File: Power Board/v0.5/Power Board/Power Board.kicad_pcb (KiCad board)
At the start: 4 copper layers, 70 x 80 mm, 91 parts, among them J1 Battery In, J2 JST B2PS-VH, J3 JST B2PS-VH, J4 JST B2PS-VH, J5 JST B2PS-VH, J6 JST B2PS-VH, J7 JST B2PS-VH, J9 Raspberry Pi, Q1 SI5504BDC, SW1 SW_Push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

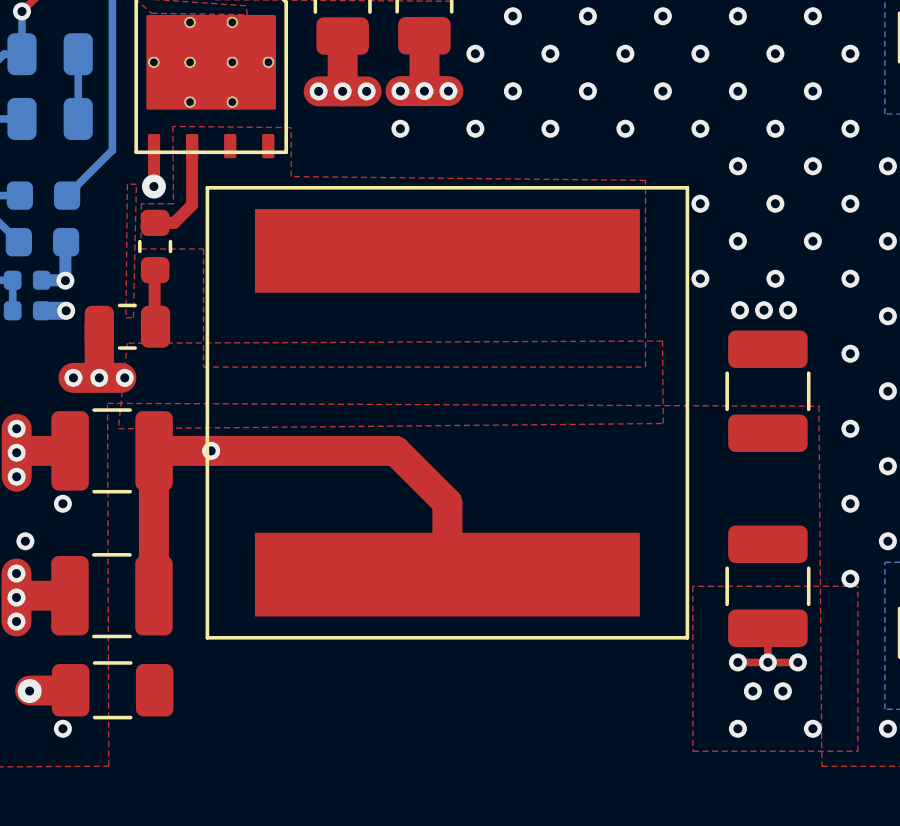
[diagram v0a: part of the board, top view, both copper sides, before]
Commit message: Correct Coilcraft XAL1580 footprint: enlarge pads, break up paste areas.
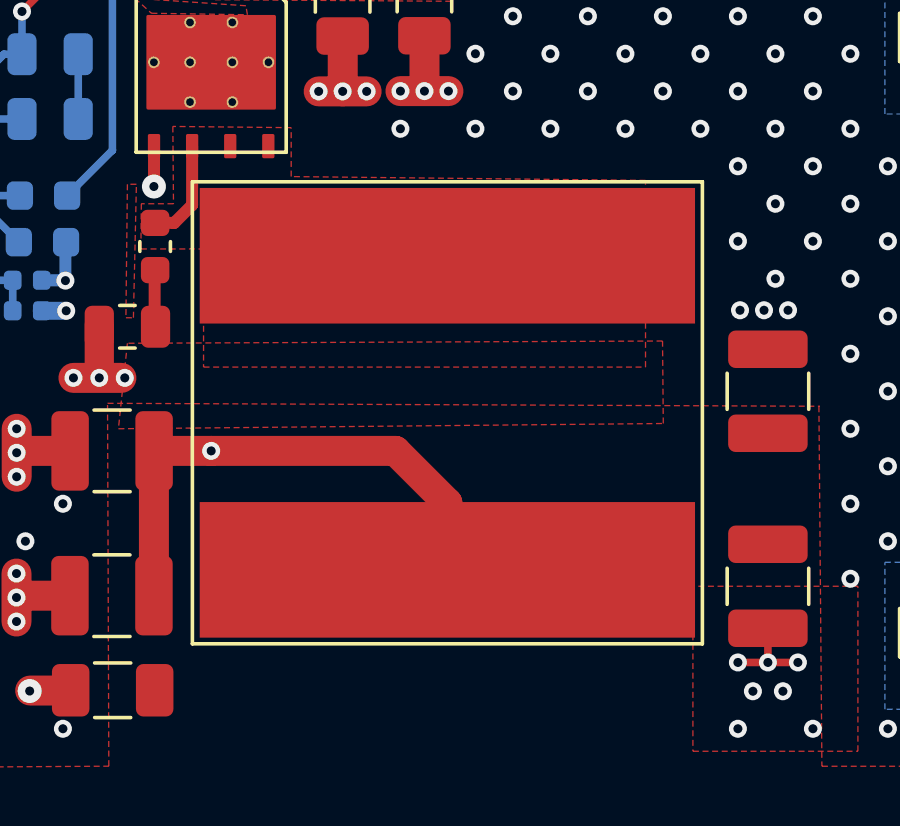
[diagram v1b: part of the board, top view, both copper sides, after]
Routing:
- net GND: vias 272 -> 270
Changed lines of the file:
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@@
     (thickness 1.6)
     (drawings 25)
-    (tracks 900)
+    (tracks 898)
     (zones 0)
     (modules 91)
@@
     (1 In1.Cu signal)
     (2 In2.Cu signal)
-    (31 B.Cu signal)
+    (31 B.Cu signal hide)
     (32 B.Adhes user hide)
     (33 F.Adhes user hide)
@@
     (35 F.Paste user hide)
     (36 B.SilkS user)
-    (37 F.SilkS user hide)
+    (37 F.SilkS user)
     (38 B.Mask user)
     (39 F.Mask user hide)
@@
     (45 Margin user hide)
     (46 B.CrtYd user)
-    (47 F.CrtYd user hide)
+    (47 F.CrtYd user)
     (48 B.Fab user hide)
     (49 F.Fab user hide)
@@
     (pad_to_mask_clearance 0.0508)
     (aux_axis_origin 0 0)
-    (visible_elements FFFFEFFF)
+    (visible_elements FFFEEFFF)
     (pcbplotparams
       (layerselection 0x010f0_ffffffff)
@@
     (add_net /Panel_Power)
   )
+  (module Power_Board:Coilcraft_XAL1580 (layer F.Cu)
+    (at 115.316 93.218 90)
+    (fp_text reference L8 (at 0 5.08 90) (layer F.SilkS) hide
+      (effects (font (size 1 1) (thickness 0.15)))
+    )
+    (fp_text value 1.3µH (at 0 -5.08 90) (layer F.Fab)
+      (effects (font (size 1 1) (thickness 0.15)))
+    )
+    (fp_line (start 8 8.8) (end 8 -8.8) (layer F.CrtYd) (width 0.12))
+    (fp_line (start -8 8.8) (end 8 8.8) (layer F.CrtYd) (width 0.12))
+    (fp_line (start -8 -8.8) (end -8 8.8) (layer F.CrtYd) (width 0.12))
+    (fp_line (start 8 -8.8) (end -8 -8.8) (layer F.CrtYd) (width 0.12))
+    (fp_line (start 7.7 8.5) (end 7.7 -8.5) (layer F.SilkS) (width 0.12))
+    (fp_line (start -7.7 8.5) (end 7.7 8.5) (layer F.SilkS) (width 0.12))
+    (fp_line (start -7.7 -8.5) (end -7.7 8.5) (layer F.SilkS) (width 0.12))
+    (fp_line (start 7.7 -8.5) (end -7.7 -8.5) (layer F.SilkS) (width 0.12))
+    (pad 2 smd roundrect (at -5.235 6.19125 90) (size 3 3) (layers F.Cu F.Paste) (roundrect_rratio 0.25)
+      (net 13 /Panel_Power))
+    (pad 2 smd roundrect (at -5.235 2.05 90) (size 3 3) (layers F.Cu F.Paste) (roundrect_rratio 0.25)
+      (net 13 /Panel_Power))
+    (pad 2 smd roundrect (at -5.235 -2.0635 90) (size 3 3) (layers F.Cu F.Paste) (roundrect_rratio 0.25)
+      (net 13 /Panel_Power))
+    (pad 2 smd roundrect (at -5.235 -6.1915 90) (size 3 3) (layers F.Cu F.Paste) (roundrect_rratio 0.25)
+      (net 13 /Panel_Power))
+    (pad 1 smd roundrect (at 5.235 6.19135 90) (size 3 3) (layers F.Cu F.Paste) (roundrect_rratio 0.25)
+      (net 41 "/Panel Power/Switch_Node"))
+    (pad 1 smd roundrect (at 5.235 2.06375 90) (size 3 3) (layers F.Cu F.Paste) (roundrect_rratio 0.25)
+      (net 41 "/Panel Power/Switch_Node"))
+    (pad 1 smd roundrect (at 5.235 -2.0635 90) (size 3 3) (layers F.Cu F.Paste) (roundrect_rratio 0.25)
+      (net 41 "/Panel Power/Switch_Node"))
+    (pad 1 smd roundrect (at 5.235 -6.1915 90) (size 3 3) (layers F.Cu F.Paste) (roundrect_rratio 0.25)
+      (net 41 "/Panel Power/Switch_Node"))
+    (pad 2 smd rect (at -5.235 0 90) (size 4.52 16.51) (layers F.Cu F.Mask)
+      (net 13 /Panel_Power))
+    (pad 1 smd rect (at 5.235 0 90) (size 4.52 16.51) (layers F.Cu F.Mask)
+      (net 41 "/Panel Power/Switch_Node"))
+    (model "${KIPRJMOD}/../Power Board Models/Coilcraft-XAL1580-102.step"
+      (at (xyz 0 0 0))
+      (scale (xyz 1 1 1))
+      (rotate (xyz -90 0 180))
+    )
+  )
   (module Resistor_SMD:R_0603_1608Metric (layer B.Cu)
     (at 93.25 89 180)
@@
       (xy -10.406932 -8.555676)) (layer B.Mask) (width 0.01))
   )
-  (module Power_Board:Coilcraft_XAL1580 (layer F.Cu)
-    (at 115.316 93.218 90)
-    (fp_text reference L8 (at 0 5.08 90) (layer F.SilkS) hide
-      (effects (font (size 1 1) (thickness 0.15)))
-    )
-    (fp_text value 1.3µH (at 0 -5.08 90) (layer F.Fab)
-      (effects (font (size 1 1) (thickness 0.15)))
-    )
-    (fp_line (start 7.75 8.25) (end 7.75 -8.25) (layer F.CrtYd) (width 0.12))
-    (fp_line (start -7.75 8.25) (end 7.75 8.25) (layer F.CrtYd) (width 0.12))
-    (fp_line (start -7.75 -8.25) (end -7.75 8.25) (layer F.CrtYd) (width 0.12))
-    (fp_line (start 7.75 -8.25) (end -7.75 -8.25) (layer F.CrtYd) (width 0.12))
-    (fp_line (start 7.5 8) (end 7.5 -8) (layer F.SilkS) (width 0.12))
-    (fp_line (start -7.5 8) (end 7.5 8) (layer F.SilkS) (width 0.12))
-    (fp_line (start -7.5 -8) (end -7.5 8) (layer F.SilkS) (width 0.12))
-    (fp_line (start 7.5 -8) (end -7.5 -8) (layer F.SilkS) (width 0.12))
-    (pad 2 smd rect (at -5.395 0 90) (size 2.79 12.83) (layers F.Cu F.Paste F.Mask)
-      (net 13 /Panel_Power))
-    (pad 1 smd rect (at 5.395 0 90) (size 2.79 12.83) (layers F.Cu F.Paste F.Mask)
-      (net 41 "/Panel Power/Switch_Node"))
-    (model "${KIPRJMOD}/../Power Board Models/Coilcraft-XAL1580-102.step"
-      (at (xyz 0 0 0))
-      (scale (xyz 1 1 1))
-      (rotate (xyz -90 0 180))
-    )
-  )
   (module Power_Board:Fuse_1206_3216Metric (layer F.Cu)
     (at 138.2 91.3)
@@
   (via (at 133.75 88.75) (size 0.6) (drill 0.3) (layers F.Cu B.Cu) (net 4))
   (via (at 126.25 88.75) (size 0.6) (drill 0.3) (layers F.Cu B.Cu) (net 4))
-  (via (at 123.75 88.75) (size 0.6) (drill 0.3) (layers F.Cu B.Cu) (net 4))
   (via (at 125 87.5) (size 0.6) (drill 0.3) (layers F.Cu B.Cu) (net 4))
   (via (at 127.5 87.5) (size 0.6) (drill 0.3) (layers F.Cu B.Cu) (net 4))
@@
   (via (at 128.75 86.25) (size 0.6) (drill 0.3) (layers F.Cu B.Cu) (net 4))
   (via (at 126.25 86.25) (size 0.6) (drill 0.3) (layers F.Cu B.Cu) (net 4))
-  (via (at 123.75 86.25) (size 0.6) (drill 0.3) (layers F.Cu B.Cu) (net 4))
   (via (at 125 85) (size 0.6) (drill 0.3) (layers F.Cu B.Cu) (net 4))
   (via (at 127.5 85) (size 0.6) (drill 0.3) (layers F.Cu B.Cu) (net 4))

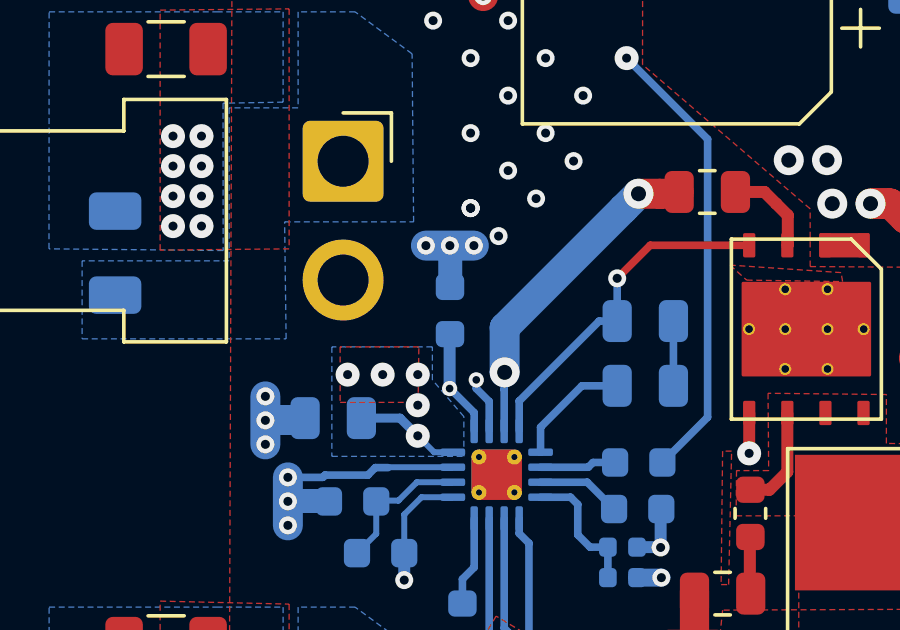
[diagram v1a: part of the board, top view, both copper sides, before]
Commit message: Correct C14 footprint, remove C6 and C9 incorrect package.
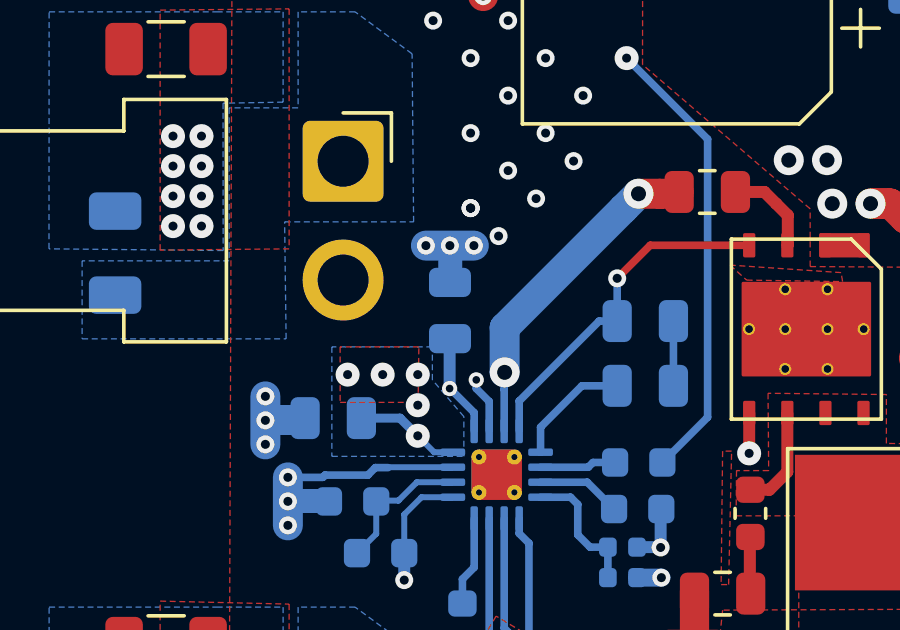
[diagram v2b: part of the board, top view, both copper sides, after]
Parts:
- C14: footprint Capacitor_SMD:C_0603_1608Metric -> Capacitor_SMD:C_0805_2012Metric
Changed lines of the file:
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@@
   (layers
     (0 F.Cu signal)
-    (1 In1.Cu signal)
-    (2 In2.Cu signal)
-    (31 B.Cu signal hide)
+    (1 In1.Cu signal hide)
+    (2 In2.Cu signal hide)
+    (31 B.Cu signal)
     (32 B.Adhes user hide)
     (33 F.Adhes user hide)
@@
     (pad_to_mask_clearance 0.0508)
     (aux_axis_origin 0 0)
-    (visible_elements FFFEEFFF)
+    (visible_elements FFFFEFFF)
     (pcbplotparams
       (layerselection 0x010f0_ffffffff)
@@
     (add_net /Panel_Power)
   )
+  (module Capacitor_SMD:C_0805_2012Metric (layer B.Cu)
+    (at 95.563 80.914 90)
+    (descr "Capacitor SMD 0805 (2012 Metric), square (rectangular) end terminal, IPC_7351 nominal, (Body size source: https://docs.google.com/spreadsheets/d/1BsfQQcO9C6DZCsRaXUlFlo91Tg2WpOkGARC1WS5S8t0/edit?usp=sharing), generated with kicad-footprint-generator")
+    (tags capacitor)
+    (attr smd)
+    (fp_text reference C14 (at 0 1.65 90) (layer B.SilkS)
+      (effects (font (size 1 1) (thickness 0.15)) (justify mirror))
+    )
+    (fp_text value 1µF (at 0 -1.65 90) (layer B.Fab)
+      (effects (font (size 1 1) (thickness 0.15)) (justify mirror))
+    )
+    (fp_text user %R (at 0 0 90) (layer B.Fab)
+      (effects (font (size 0.5 0.5) (thickness 0.08)) (justify mirror))
+    )
+    (fp_line (start 1.68 -0.95) (end -1.68 -0.95) (layer B.CrtYd) (width 0.05))
+    (fp_line (start 1.68 0.95) (end 1.68 -0.95) (layer B.CrtYd) (width 0.05))
+    (fp_line (start -1.68 0.95) (end 1.68 0.95) (layer B.CrtYd) (width 0.05))
+    (fp_line (start -1.68 -0.95) (end -1.68 0.95) (layer B.CrtYd) (width 0.05))
+    (fp_line (start -0.258578 -0.71) (end 0.258578 -0.71) (layer B.SilkS) (width 0.12))
+    (fp_line (start -0.258578 0.71) (end 0.258578 0.71) (layer B.SilkS) (width 0.12))
+    (fp_line (start 1 -0.6) (end -1 -0.6) (layer B.Fab) (width 0.1))
+    (fp_line (start 1 0.6) (end 1 -0.6) (layer B.Fab) (width 0.1))
+    (fp_line (start -1 0.6) (end 1 0.6) (layer B.Fab) (width 0.1))
+    (fp_line (start -1 -0.6) (end -1 0.6) (layer B.Fab) (width 0.1))
+    (pad 2 smd roundrect (at 0.9375 0 90) (size 0.975 1.4) (layers B.Cu B.Paste B.Mask) (roundrect_rratio 0.25)
+      (net 4 GND))
+    (pad 1 smd roundrect (at -0.9375 0 90) (size 0.975 1.4) (layers B.Cu B.Paste B.Mask) (roundrect_rratio 0.25)
+      (net 9 "/Panel Power/Vreg"))
+    (model ${KISYS3DMOD}/Capacitor_SMD.3dshapes/C_0805_2012Metric.wrl
+      (at (xyz 0 0 0))
+      (scale (xyz 1 1 1))
+      (rotate (xyz 0 0 0))
+    )
+  )
   (module Power_Board:Coilcraft_XAL1580 (layer F.Cu)
     (at 115.316 93.218 90)
@@
     )
   )
-  (module Capacitor_SMD:C_0603_1608Metric (layer B.Cu)
-    (at 95.563 80.914 90)
-    (descr "Capacitor SMD 0603 (1608 Metric), square (rectangular) end terminal, IPC_7351 nominal, (Body size source: http://www.tortai-tech.com/upload/download/2011102023233369053.pdf), generated with kicad-footprint-generator")
-    (tags capacitor)
-    (attr smd)
-    (fp_text reference C14 (at 0 1.43 90) (layer B.SilkS) hide
-      (effects (font (size 1 1) (thickness 0.15)) (justify mirror))
-    )
-    (fp_text value 1µF (at 0 -1.43 90) (layer B.Fab)
-      (effects (font (size 1 1) (thickness 0.15)) (justify mirror))
-    )
-    (fp_text user %R (at 0 0 90) (layer B.Fab)
-      (effects (font (size 0.4 0.4) (thickness 0.06)) (justify mirror))
-    )
-    (fp_line (start 1.48 -0.73) (end -1.48 -0.73) (layer B.CrtYd) (width 0.05))
-    (fp_line (start 1.48 0.73) (end 1.48 -0.73) (layer B.CrtYd) (width 0.05))
-    (fp_line (start -1.48 0.73) (end 1.48 0.73) (layer B.CrtYd) (width 0.05))
-    (fp_line (start -1.48 -0.73) (end -1.48 0.73) (layer B.CrtYd) (width 0.05))
-    (fp_line (start -0.162779 -0.51) (end 0.162779 -0.51) (layer B.SilkS) (width 0.12))
-    (fp_line (start -0.162779 0.51) (end 0.162779 0.51) (layer B.SilkS) (width 0.12))
-    (fp_line (start 0.8 -0.4) (end -0.8 -0.4) (layer B.Fab) (width 0.1))
-    (fp_line (start 0.8 0.4) (end 0.8 -0.4) (layer B.Fab) (width 0.1))
-    (fp_line (start -0.8 0.4) (end 0.8 0.4) (layer B.Fab) (width 0.1))
-    (fp_line (start -0.8 -0.4) (end -0.8 0.4) (layer B.Fab) (width 0.1))
-    (pad 2 smd roundrect (at 0.7875 0 90) (size 0.875 0.95) (layers B.Cu B.Paste B.Mask) (roundrect_rratio 0.25)
-      (net 4 GND))
-    (pad 1 smd roundrect (at -0.7875 0 90) (size 0.875 0.95) (layers B.Cu B.Paste B.Mask) (roundrect_rratio 0.25)
-      (net 9 "/Panel Power/Vreg"))
-    (model ${KISYS3DMOD}/Capacitor_SMD.3dshapes/C_0603_1608Metric.wrl
-      (at (xyz 0 0 0))
-      (scale (xyz 1 1 1))
-      (rotate (xyz 0 0 0))
-    )
-  )
   (module Capacitor_SMD:C_1206_3216Metric (layer F.Cu)
     (at 111.824 79.259 270)
@@
   (segment (start 119.6085 53.848) (end 118.491 53.848) (width 0.8) (layer B.Cu) (net 4))
   (segment (start 111.827 80.765) (end 111.827 82.502) (width 1) (layer F.Cu) (net 4))
-  (segment (start 95.571 80.013) (end 95.571 78.812) (width 0.8) (layer B.Cu) (net 4))
   (via (at 140.716 49.784) (size 0.6) (drill 0.3) (layers F.Cu B.Cu) (net 4))
   (segment (start 141.873 49.784) (end 140.716 49.784) (width 0.254) (layer F.Cu) (net 4))
@@
   (via (at 98.43253 77.18253) (size 0.6) (drill 0.3) (layers F.Cu B.Cu) (net 4))
   (via (at 97.18253 78.43253) (size 0.6) (drill 0.3) (layers F.Cu B.Cu) (net 4))
+  (segment (start 95.571 79.9765) (end 95.571 78.812) (width 0.8) (layer B.Cu) (net 4))
   (via (at 101.450002 72.5) (size 0.8) (drill 0.3) (layers F.Cu B.Cu) (net 5))
   (segment (start 126.32 45.129) (end 126.32 45.13) (width 0.254) (layer B.Cu) (net 5))
@@
   (segment (start 95.588 81.7265) (end 95.563 81.7015) (width 0.254) (layer B.Cu) (net 9))
   (segment (start 95.55 81.7145) (end 95.563 81.7015) (width 0.254) (layer B.Cu) (net 9))
-  (segment (start 95.55 83.514) (end 95.55 81.7145) (width 0.4) (layer B.Cu) (net 9))
   (segment (start 102.072 88.3) (end 96.159 88.3) (width 0.4) (layer In2.Cu) (net 9))
   (segment (start 95.758 84.709) (end 95.55 84.501) (width 0.4) (layer In2.Cu) (net 9))
@@
   (segment (start 96.369 84.319) (end 96.369 84.9245) (width 0.254) (layer B.Cu) (net 9))
   (segment (start 95.588 83.514) (end 95.588 83.538) (width 0.254) (layer B.Cu) (net 9))
+  (segment (start 95.55 83.514) (end 95.55 81.8515) (width 0.4) (layer B.Cu) (net 9))
   (segment (start 103.0105 83.424) (end 103.0105 81.265) (width 0.254) (layer B.Cu) (net 10))
   (via (at 101.1355 79.84001) (size 0.6) (drill 0.3) (layers F.Cu B.Cu) (net 11))
